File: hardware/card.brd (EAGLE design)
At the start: 160 x 100 mm, 56 parts, among them J1 UE27AC54100, J2 B2PS-VH(LF)(SN), J3 MINI-USB-UX60A-MB-5ST, J4 MICROSD, U1 ATSAMD21J_QFN, U3 TLV70233DBVR, U4 ATWINC1500_MR210PA, U5 NHD-C12832A1Z-FSW-FBW-3V3, U6 MIC2288YD5-TR, X3 32.768

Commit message: add framing for software components. Design review schematic tweaks
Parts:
- removed CN1: (no value), lib-card:JSTPH2
- removed T1: (no value), CardReader:SOT-23
- added C16, C23, C24: 10uF, rcl:C0603
- added C17, C18, C19, C20, C21: 0.1uF, rcl:C0603
- added C22, C25, C26, C27: 1uF, rcl:C0603
- added D7: RED, led:SMARTLED-TTW
- added F1: 2A, RoboJackets-Fuses:F0603
- added F2: 500mA, RoboJackets-Fuses:F0603
- added J5: JST_2PIN, CardReader:JSTPH2
- added R17: 2.2k, RoboJackets-Resistors:R0603W
- added R18: 100k, RoboJackets-Resistors:R0603W
- added R19: 10k, RoboJackets-Resistors:R0603W
- added U7: TS3USB221, CardReader:10-PIN-UQFN
- C14: value 4.7uF -> 10uF
- C15: value 22uF -> 10uF
- C9: value (none) -> 0.1uF
- J4: device lib-card:MICROSD -> CardReader:MICROSD
- R1, R2, R3: value 150 -> 330
- R16: value 10k -> 0; device rcl:R0603 -> RoboJackets-Resistors:R0603W
- R6, R8: value 100k 1% -> 10k 1%
- U1: device lib-card:TQFN48_7MM -> CardReader:TQFN48_7MM
- U2: value (none) -> MCP73833; device lib-card:MSOP10 -> CardReader:MSOP10
- U4: device lib-card:ATWINC1500_MR210PA -> CardReader:ATWINC1500_MR210PA
- moved R16 150.5 mm to (-61.5, -291.0)
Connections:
- removed net BOOST_ENABLE: R16.1, T1.1, U6.4
- new net 1D+: J3.3, U7.1
- new net 1D-: J3.2, U7.2
- new net 2D+: J1.3, U7.3
- new net 2D-: J1.2, U7.4
- new net BATT-PRE-FUSE: F1.2, J5.1
- new net N$11: C16.1, R16.1, U5.LED+
- new net N$13: R18.2, R19.2, U7.9
- new net PROG-LED: D7.A@1, R17.2
- new net PROG-LED-2: R17.1, U1.26
- net +3.3V: now also C21.1, C22.1, R16.2, U7.10; no longer U5.LED+
- net +5V: now also C26.1, C3.1, J3.1; no longer T1.3
- net BATT: now also C27.2, F1.1; no longer CN1.1
- net BTN-DOWN: now also C18.1
- net BTN-LEFT: now also C19.1
- net BTN-RIGHT: now also C20.1, U1.4; no longer U1.26
- net BTN-UP: now also C17.1
- net D+: now also U7.8; no longer J1.3, J3.3
- net D-: now also U7.7; no longer J1.2, J3.2
- net GND: now also C17.2, C18.2, C19.2, C20.2, C21.2, C22.2, C23.2, C24.2, C25.2, C26.2, C27.1, D7.C@1, J5.2, R18.1, U7.5, U7.6; no longer CN1.2, T1.2
- net N$27: now also U5.C1+
- net N$29: now also C15.1, C23.1, C24.1, D6.C, F2.1, R14.2; no longer C3.1, J3.1
- net USB-HOST-EN: now also R19.1
- net VBATT: now also C25.1, U6.4; no longer R16.2
- net VBUS: now also F2.2; no longer C15.1, D6.C, R14.2

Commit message: Schematic Finished
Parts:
- removed U5: NHD-C12832A1Z-FSW-FBW-3V3, CardReader:NHD-C12832A1Z-FSW-FBW-3V3
- added C28, C29, C30, C32: 0.1uF, rcl:C0603
- added C31: 1uF, rcl:C0603
- added J6: 0541323062, CardReader:0541323062
- added J7: JST_2PIN, card:JSTPH2
- added S6: KAE01SGGT, CardReader:KAE01SGGT
- C1, C10, C2, C8: value 0.1uF -> 1uF
- C11, C12, C13: value 2.2uF -> 0.1uF
- C16: value 10uF -> 1uF
- moved C1 315.6 mm to (-66.5, -386.0)
- moved C2 315.6 mm to (-66.5, -389.5)
- moved C8 315.6 mm to (-66.5, -393.0)
- moved C9 315.6 mm to (-66.5, -396.5)
- moved C11 312.1 mm to (-66.5, -400.0)
- moved C12 312.1 mm to (-66.5, -403.5)
- moved C13 312.1 mm to (-66.5, -407.0)
- moved C16 128.9 mm to (-76.5, -422.5)
- moved R16 128.9 mm to (-76.5, -419.0)
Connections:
- removed net N$11: C16.1, R16.1, U5.LED+
- removed net N$13: R18.2, R19.2, U7.9
- removed net N$19: C1.1, U5.V0
- removed net N$20: C8.1, U5.V2
- removed net N$21: C10.1, U5.V3
- removed net N$22: C2.1, U5.V1
- removed net N$23: C9.1, U5.V4
- removed net N$24: C11.1, U5.C2+
- removed net N$25: C11.2, U5.C2-
- removed net N$26: C13.1, U5.V_OUT
- removed net N$27: C12.1, U5.C1+
- removed net N$28: C12.2, U5.C1-
- removed net SCR-!CS: U1.25, U5.!CS1
- removed net SCR-!RST: U1.24, U5.!RST
- removed net SCR-REG: U1.16, U5.A0
- new net LCD-!CS: J6.1, U1.29
- new net LCD-!RES: J6.2, U1.31
- new net LCD-A0: J6.3, U1.48
- new net LCD-CA1+: C2.1, J6.18
- new net LCD-CA1-: C1.2, C2.2, J6.17
- new net LCD-CA2+: C8.1, J6.19
- new net LCD-CA2-: C8.2, J6.20
- new net LCD-CA3+: C1.1, J6.16
- new net LCD-K: J7.2, R16.1
- new net LCD-MOSI: J6.13, U1.37
- new net LCD-SCK: J6.12, U1.38
- new net LCD-V0: C28.1, J6.27
- new net LCD-V1: C13.1, J6.26
- new net LCD-V2: C12.1, J6.25
- new net LCD-V3: C11.1, J6.24
- new net LCD-V4: C9.1, J6.23
- new net LCD-VOUT: C10.1, J6.15
- new net USB-S: R18.2, R19.2, S6.1, U7.9
- net +3.3V: now also C16.1, C29.1, C30.1, C31.1, C32.1, J6.22, J6.4, J6.5, J7.1; no longer R16.2, U5.V_DD
- net BTN-LEFT: now also U1.25; no longer U1.29
- net BTN-RIGHT: now also U1.24; no longer U1.4
- net GND: now also C11.2, C12.2, C16.2, C28.2, C29.2, C30.2, C31.2, C32.2, J6.10, J6.11, J6.14, J6.21, J6.29, J6.30, J6.6, J6.7, J6.8, J6.9, R16.2, S6.2; no longer C1.2, C2.2, C8.2, U5.LED-, U5.V_SS
- net MOSI: no longer U5.SI
- net SCK: no longer U5.SCL

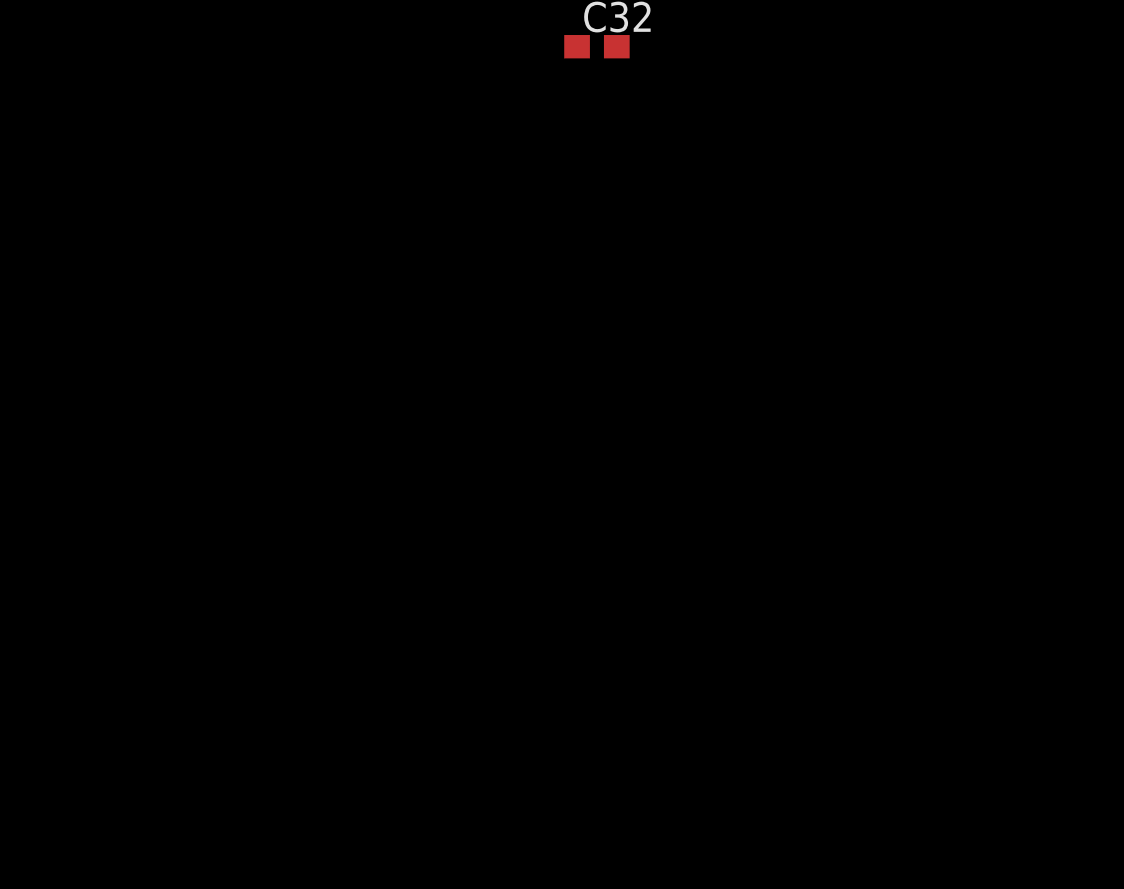
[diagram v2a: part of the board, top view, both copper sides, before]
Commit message: Added power test points and LEDs
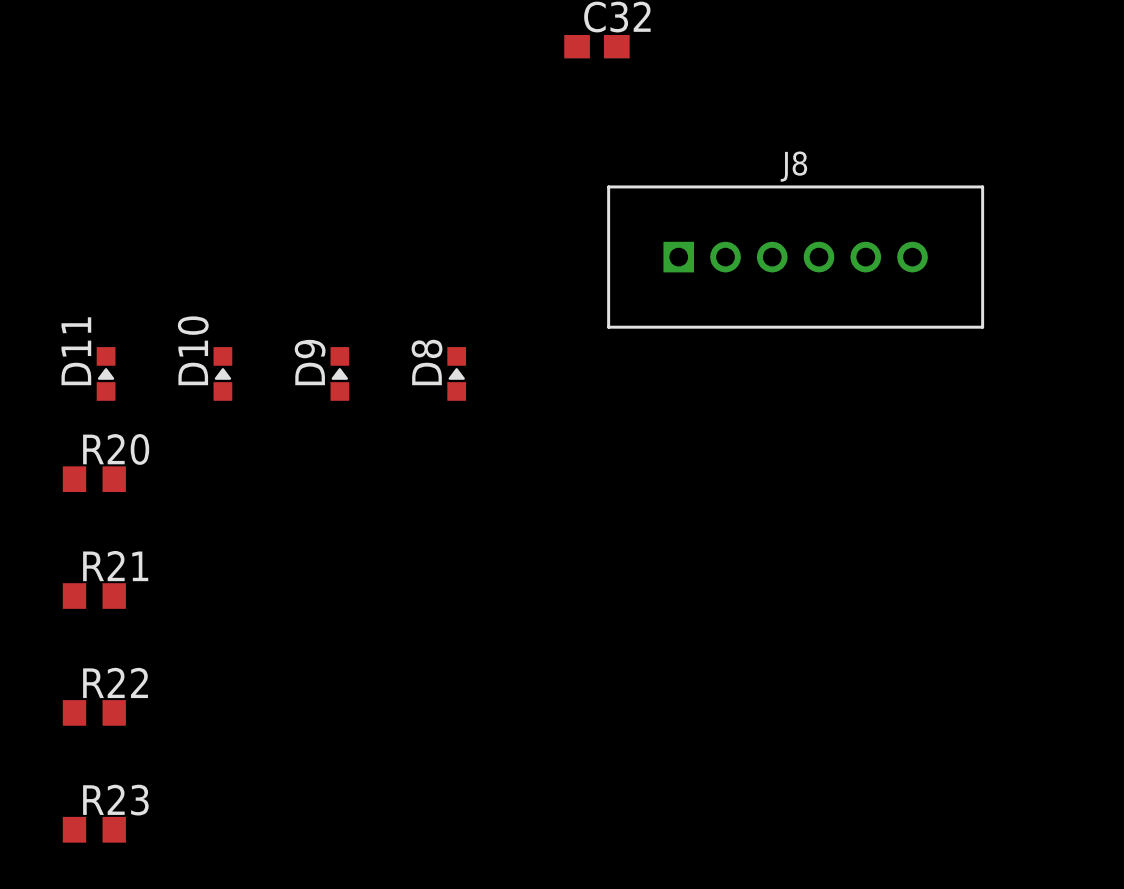
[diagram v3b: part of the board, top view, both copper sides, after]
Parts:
- added D10: YELLOW, lib-card:CHIP-LED0603
- added D11: RED, lib-card:CHIP-LED0603
- added D8, D9: GREEN, lib-card:CHIP-LED0603
- added J8: 6-PIN_2MM-V, RoboJackets-Connectors:2MM-6-V
- added R20, R21, R22, R23: 1k, rcl:R0603
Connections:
- net N$1 renamed LED-STAT2
- net N$14 renamed VDDCORE
- net N$15 renamed X3-1
- net N$16 renamed X3-2
- net N$17 renamed WIFI-LED-Y
- net N$18 renamed WIFI-LED-G
- net N$2 renamed LED-STAT1
- net N$29 renamed BOOST_OUTPUT
- net N$6 renamed LED-!PG
- new net LED-3V3: D9.A, R21.2
- new net LED-5V: D11.A, R23.2
- new net LED-VBATT: D10.A, R22.2
- new net LED-VBUS: D8.A, R20.2
- net +3.3V: now also J6.26, J6.27, J6.9, J8.3, R21.1; no longer J6.22, J6.4, J6.5
- net +5V: now also J8.6, R23.1
- net GND: now also D10.C, D11.C, D8.C, D9.C, J6.1, J6.17, J6.2, J6.20, J6.22, J6.23, J6.24, J6.25, J8.1; no longer J6.11, J6.14, J6.29, J6.30, J6.6, J6.7, J6.8, J6.9
- net LCD-!CS: now also J6.30; no longer J6.1
- net LCD-!RES: now also J6.29; no longer J6.2
- net LCD-A0: now also J6.28; no longer J6.3
- net LCD-CA1+: now also J6.13; no longer J6.18
- net LCD-CA1-: now also J6.14; no longer J6.17
- net LCD-CA2+: now also J6.12; no longer J6.19
- net LCD-CA2-: now also J6.11; no longer J6.20
- net LCD-CA3+: now also J6.15; no longer J6.16
- net LCD-MOSI: now also J6.18; no longer J6.13
- net LCD-SCK: now also J6.19; no longer J6.12
- net LCD-V0: now also J6.4; no longer J6.27
- net LCD-V1: now also J6.5; no longer J6.26
- net LCD-V2: now also J6.6; no longer J6.25
- net LCD-V3: now also J6.7; no longer J6.24
- net LCD-V4: now also J6.8; no longer J6.23
- net LCD-VOUT: now also J6.16; no longer J6.15
- net VBATT: now also J8.4, R22.1
- net VBUS: now also J8.5, R20.1

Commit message: halfway through routing
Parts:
- D11: value RED -> GREEN
- D8: value GREEN -> RED
- moved R23 532.3 mm to (27.5, 39.5), flipped to the bottom, turned to 270 degrees
- moved R22 526.4 mm to (23.5, 39.5), flipped to the bottom, turned to 270 degrees
- moved R21 521.1 mm to (21.5, 39.5), flipped to the bottom, turned to 270 degrees
- moved C31 518.9 mm to (45.0, 67.0), flipped to the bottom, turned to 270 degrees
- moved R20 517.2 mm to (25.5, 39.5), flipped to the bottom, turned to 270 degrees
- moved C30 514.4 mm to (46.5, 67.0), flipped to the bottom, turned to 270 degrees
- moved C29 512.7 mm to (55.0, 68.0), flipped to the bottom, turned to 180 degrees
- moved C16 509.3 mm to (55.0, 69.5), flipped to the bottom, turned to 180 degrees
- moved D11 508.0 mm to (27.5, 34.0), flipped to the bottom, turned to 180 degrees
- moved S6 505.7 mm to (56.0, 54.0), flipped to the bottom
- moved D10 505.7 mm to (23.5, 34.0), flipped to the bottom, turned to 180 degrees
- moved J8 504.5 mm to (21.5, 43.5)
- moved D9 504.0 mm to (21.5, 34.0), flipped to the bottom, turned to 180 degrees
- moved D8 503.8 mm to (25.5, 34.0), flipped to the bottom, turned to 180 degrees
- moved C32 472.1 mm to (37.0, 14.0), turned to 90 degrees
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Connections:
- net N$10 renamed WIFI-GPIO15
- net N$3 renamed CHRG-STAT1
- net N$4 renamed CHRG-STAT2
- net N$5 renamed CHRG-!PG
- net N$7 renamed CHRG-PROG
- net N$8 renamed CHRG-THERM
- removed net N$9: R11.2, U4.J27
- new net WIFI-GPIO16: R11.1, U4.J27
- net +5V: now also J8.5, R20.1; no longer J8.6, R23.1
- net VBUS: now also J8.6, R23.1; no longer J8.5, R20.1
- net WIFI-LED-Y: now also R11.2; no longer R11.1
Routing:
- net +3.3V: track 0.00 -> 82.3 mm, vias 0 -> 5
- net WIFI-!IRQ: track 0.00 -> 77.6 mm, vias 0 -> 3
- net GND: track 0.00 -> 75.2 mm, vias 0 -> 22
- net WIFI-CHIP-EN: track 0.00 -> 73.9 mm, vias 0 -> 1
- net VBATT: track 0.00 -> 70.0 mm, vias 0 -> 2
- net +5V: track 0.00 -> 67.9 mm, vias 0 -> 3
- net 1D+: track 0.00 -> 47.6 mm, vias 0 -> 1
- net 1D-: track 0.00 -> 46.2 mm, vias 0 -> 1
- net BATT: track 0.00 -> 40.5 mm, vias 0 -> 1
- net LCD-!RES: track 0.00 -> 33.5 mm
- net LCD-!CS: track 0.00 -> 30.7 mm
- net 2D-: track 0.00 -> 29.9 mm
- net 2D+: track 0.00 -> 27.6 mm
- net USB-HOST-EN: track 0.00 -> 16.3 mm, vias 0 -> 1
- net BOOST_OUTPUT: track 0.00 -> 14.6 mm
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- added copper zone on layer 16, net GND
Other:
- board size 160 x 100 mm -> 100 x 100 mm

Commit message: basically done routing attempt 1
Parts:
- moved J4 7.00 mm to (33.1, 80.9)
- moved C21 7.00 mm to (26.5, 87.0)
- moved C22 7.00 mm to (26.5, 85.0)
- moved C19 5.15 mm to (77.0, 66.5)
- moved C20 4.27 mm to (92.0, 66.5), turned to 180 degrees
- moved R16 3.64 mm to (59.5, 16.5), turned to 90 degrees
- moved C18 2.69 mm to (83.5, 57.5), turned to 270 degrees
- moved C17 1.12 mm to (84.0, 82.5), turned to 90 degrees
- moved R9 1.12 mm to (12.7, 2.92)
- moved C32 0.56 mm to (36.8, 13.5)
- moved U4 0.14 mm to (8.25, 13.5)
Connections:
- net BTN-LEFT: now also U1.27; no longer U1.25
- net BTN-RIGHT: now also U1.25; no longer U1.24
- net BTN-UP: now also U1.24; no longer U1.27
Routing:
- net +3.3V: track 82.3 -> 252.1 mm, vias 5 -> 16
- net MOSI: track 6.57 -> 107.5 mm, vias 1 -> 6
- net VBUS: track 3.15 -> 101.4 mm, vias 0 -> 6
- net MISO: track 6.57 -> 102.7 mm, vias 1 -> 6
- net SCK: track 6.98 -> 101.2 mm, vias 1 -> 6
- net WIFI-!CS: track 0.00 -> 79.3 mm, vias 0 -> 5
- net LCD-A0: track 6.22 -> 72.0 mm, vias 0 -> 2
- net BTN-DOWN: track 3.02 -> 64.2 mm, vias 1 -> 3
- net BTN-UP: track 3.98 -> 64.7 mm, vias 1 -> 3
- net BTN-RIGHT: track 2.19 -> 60.9 mm, vias 1 -> 3
- net LCD-SCK: track 9.41 -> 62.6 mm
- net LCD-MOSI: track 8.41 -> 61.6 mm
- net BTN-LEFT: track 1.48 -> 49.3 mm, vias 1 -> 3
- net SD-!CS: track 0.00 -> 31.7 mm, vias 0 -> 1
- net LCD-!CS: track 30.7 -> 59.4 mm, vias 0 -> 2
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
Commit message: board routing attempt 2
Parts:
- removed U6: MIC2288YD5-TR, CardReader:TSOT-23-5
- removed U7: TS3USB221, CardReader:10-PIN-UQFN
- added C33: 1uF, rcl:C0603
- added U5: TLV70233DBVR, lib-card:SOT-23-5
- added X2: 32.768, lib-card:XTAL3215
- C1, C16, C2, C25: value 1uF -> 0.1uF
- C10, C8: value 1uF -> 22pF
- C14, C15: value 10uF -> 0.1uF
- C19, C30, C32, C9: value 0.1uF -> 1uF
- C23, C24: value 10uF -> 1uF
- C26, C27: value 1uF -> 10uF
- C28, C29: value 0.1uF -> 10uF
- C3: value 10uF -> 1uF; device rcl:C0805 -> rcl:C0603
- C6: value 22pF -> 0.1uF
- C7: value 22pF -> 10uF; device rcl:C0603 -> rcl:C0805
- D1, D11: value GREEN -> RED; device lib-card:CHIP-LED0603 -> RoboJackets-LEDs:CHIP-LED0603
- D10, D2, D9: device lib-card:CHIP-LED0603 -> RoboJackets-LEDs:CHIP-LED0603
- D3, D8: value RED -> GREEN; device lib-card:CHIP-LED0603 -> RoboJackets-LEDs:CHIP-LED0603
- D4: value YELLOW -> PMEG4010EGWX; device led:SMARTLED-TTW -> CardReader:SOD123
- D5: device led:SMARTLED-TTW -> RoboJackets-LEDs:CHIP-LED0603
- D6: value PMEG4010EGWX -> GREEN; device CardReader:SOD123 -> RoboJackets-LEDs:CHIP-LED0603
- D7: value RED -> GREEN; device led:SMARTLED-TTW -> RoboJackets-LEDs:CHIP-LED0603
- F1: value 2A -> 500mA
- F2: value 500mA -> 2A
- J2: value B2PS-VH(LF)(SN) -> MICROSD; device RoboJackets-Connectors:B2PS-CENTERED -> CardReader:MICROSD
- J3: value MINI-USB-UX60A-MB-5ST -> 0541323062; device lib-card:UX60A-MB-5ST -> CardReader:0541323062
- J4: value MICROSD -> 6-PIN_2MM-V; device CardReader:MICROSD -> RoboJackets-Connectors:2MM-6-V
- J6: value 0541323062 -> B2PS-VH(LF)(SN); device CardReader:0541323062 -> RoboJackets-Connectors:B2PS-CENTERED
- J7: value JST_2PIN -> MINI-USB-UX60A-MB-5ST; device card:JSTPH2 -> lib-card:UX60A-MB-5ST
- J8: value 6-PIN_2MM-V -> JST_2PIN; device RoboJackets-Connectors:2MM-6-V -> card:JSTPH2
- R1: value 330 -> 10k
- R10, R9: value 100k -> 1k; device RoboJackets-Resistors:R0603W -> rcl:R0603
- R11, R12, R19: device RoboJackets-Resistors:R0603W -> rcl:R0603
- R13: value 0 -> 5.62k 1%
- R14: value 5.62k 1% -> 1.87k 1%
- R15: value 1.87k 1% -> 10k 1%
- R16: value 0 -> 10k 1%; device RoboJackets-Resistors:R0603W -> rcl:R0603
- R17: value 2.2k -> 330; device RoboJackets-Resistors:R0603W -> rcl:R0603
- R18: value 100k -> 330; device RoboJackets-Resistors:R0603W -> rcl:R0603
- R2: value 330 -> 100k
- R21, R4: value 1k -> 0
- R22: value 1k -> 10k
- R23: value 1k -> 330
- R3: value 330 -> 2.2k
- R5: value 10k -> 100k
- R6: value 10k 1% -> 1k
- R7: value 10k -> 1k
- R8: value 10k 1% -> 100k
- S2: value TL1000F160Q -> KAE01SGGT; device CardReader:TL1100 -> CardReader:KAE01SGGT
- S6: value KAE01SGGT -> TL1000F160Q; device CardReader:KAE01SGGT -> CardReader:TL1100
- U2: value MCP73833 -> TS3USB221; device CardReader:MSOP10 -> CardReader:10-PIN-UQFN
- U3: value TLV70233DBVR -> MIC2288YD5-TR; device lib-card:SOT-23-5 -> CardReader:TSOT-23-5
- U4: value ATWINC1500_MR210PA -> MCP73833; device CardReader:ATWINC1500_MR210PA -> CardReader:MSOP10
- X3: value 32.768 -> ATWINC1500_MR210PA; device lib-card:XTAL3215 -> CardReader:ATWINC1500_MR210PA
- moved S2 98.6 mm to (27.5, 5.00), turned to 90 degrees
- moved C22 89.3 mm to (74.2, 9.50)
- moved S5 89.2 mm to (13.0, 31.5), flipped to the bottom
- moved C21 89.2 mm to (80.5, 16.0), turned to 90 degrees
- moved J2 87.9 mm to (82.2, 21.8), flipped to the top, turned to 0 degrees
- moved R4 79.8 mm to (92.0, 18.0), turned to 90 degrees
- moved R9 79.2 mm to (86.2, 32.5), turned to 90 degrees
- moved D6 79.1 mm to (92.8, 33.8)
- moved J8 77.6 mm to (91.0, 9.00), flipped to the bottom, turned to 180 degrees
- moved J4 76.5 mm to (89.2, 29.0), flipped to the top, turned to 180 degrees
- moved C23 76.3 mm to (75.8, 13.0)
- moved C25 72.7 mm to (70.8, 16.0)
- moved R11 72.4 mm to (89.5, 32.5), turned to 90 degrees
- moved J3 71.9 mm to (75.0, 11.0), flipped to the bottom
- moved C24 71.3 mm to (74.2, 16.0), flipped to the bottom, turned to 90 degrees
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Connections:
- net !RESET: now also C6.1
- net +3.3V: now also C1.1, C11.1, C2.1, C25.1, C3.1, C33.1, C9.1, D2.A, D3.A, J2.4, J3.22, J3.4, J3.5, J4.3, J8.1, R10.1, U2.10, U5.5, X3.J10, X3.J20, X3.J23; no longer C16.1, C21.1, C22.1, C29.1, C30.1, C31.1, C32.1, D4.A@1, D5.A@1, J4.4, J6.26, J6.27, J6.9, J7.1, J8.3, R21.1, U3.5, U4.J10, U4.J20, U4.J23, U7.10
- net +5V: now also C31.1, C7.1, D10.A, D11.A, D9.A, J4.5, J7.1, R9.1, U4.1, U4.2; no longer C26.1, C3.1, D1.A, D2.A, D3.A, J3.1, J8.5, R20.1, U2.1, U2.2
- net 1D+: now also J7.3, U2.1; no longer J3.3, U7.1
- net 1D-: now also J7.2, U2.2; no longer J3.2, U7.2
- net 2D+: now also U2.3; no longer U7.3
- net 2D-: now also U2.4; no longer U7.4
- net 3V3_EN: now also R19.1, U5.3; no longer R7.1, U3.3
- net BATT: now also C32.2, F2.1, J6.2, R21.1, U4.10, U4.9; no longer C27.2, F1.1, J2.2, R13.1, U2.10, U2.9
- net BATT-MONITOR: now also R15.2, R16.1; no longer R6.2, R8.1
- net BATT-PRE-FUSE: now also F2.2; no longer F1.2
- net BOOST_FB: now also R13.1, R14.2, U3.3; no longer R14.1, R15.2, U6.3
- net BOOST_OUTPUT: now also C27.1, C28.1, C29.1, D4.C, F1.1, R13.2; no longer C15.1, C23.1, C24.1, D6.C, F2.1, R14.2
- net BOOST_SW: now also D4.A, U3.1; no longer D6.A, U6.1
- net BTN-DOWN: now also C13.1, S4.1, U1.3; no longer C18.1, S3.1, S3.2, U1.28
- net BTN-LEFT: now also C14.1, S5.1, U1.7; no longer C19.1, S4.1, S4.2, U1.27
- net BTN-RIGHT: now also C15.1, S6.2, U1.8; no longer C20.1, S5.1, S5.2, U1.25
- net BTN-UP: now also C12.1, S3.1, U1.10; no longer C17.1, S2.1, S2.2, U1.24
- net CHRG-!PG: now also R23.1, U4.7; no longer R3.1, U2.7
- net CHRG-PROG: now also R20.2, U4.6; no longer R4.2, U2.6
- net CHRG-STAT1: now also R18.1, U4.3; no longer R2.1, U2.3
- net CHRG-STAT2: now also R17.1, U4.4; no longer R1.1, U2.4
- net CHRG-THERM: now also R22.2, U4.8; no longer R5.2, U2.8
- net D+: now also U2.8; no longer U7.8
- net D-: now also U2.7; no longer U7.7
- net GND: now also C1.2, C2.2, C27.2, C32.1, C33.2, C8.2, D1.C, D5.C, D6.C, D7.C, J2.6, J2.MT1, J2.MT2, J3.10, J3.11, J3.14, J3.21, J3.29, J3.30, J3.6, J3.7, J3.8, J3.9, J4.1, J7.5, R14.1, R2.1, R20.1, R22.1, R4.2, R5.2, R8.1, S2.2, S6.3, S6.4, U2.6, U4.5, U5.2, X3.J12, X3.J28, X3.J9; no longer C19.2, C22.2, C23.2, C27.1, C32.2, D10.C, D11.C, D7.C@1, D9.C, J3.5, J4.6, J4.MT1, J4.MT2, J6.1, J6.10, J6.17, J6.2, J6.20, J6.21, J6.22, J6.23, J6.24, J6.25, J8.1, R10.2, R15.1, R18.1, R4.1, R5.1, R8.2, R9.1, S2.3, S2.4, S6.2, U4.J12, U4.J28, U4.J9, U6.2, U7.5, U7.6
- net LCD-!CS: now also J3.1, U1.23; no longer J6.30, U1.29
- net LCD-!RES: now also J3.2, U1.24; no longer J6.29, U1.31
- net LCD-A0: now also J3.3, U1.25; no longer J6.28, U1.48
- net LCD-CA1+: now also C22.1, J3.18; no longer C2.1, J6.13
- net LCD-CA1-: now also C22.2, C23.2, J3.17; no longer C1.2, C2.2, J6.14
- net LCD-CA2+: now also C19.1, J3.19; no longer C8.1, J6.12
- net LCD-CA2-: now also C19.2, J3.20; no longer C8.2, J6.11
- net LCD-CA3+: now also C23.1, J3.16; no longer C1.1, J6.15
- net LCD-K: now also J8.2, R4.1; no longer J7.2, R16.1
- net LCD-MOSI: now also J3.13; no longer J6.18
- net LCD-SCK: now also J3.12; no longer J6.19
- net LCD-V0: now also C18.1, J3.27; no longer C28.1, J6.4
- net LCD-V1: now also C21.1, J3.26; no longer C13.1, J6.5
- net LCD-V2: now also C17.1, J3.25; no longer C12.1, J6.6
- net LCD-V3: now also C20.1, J3.24; no longer C11.1, J6.7
- net LCD-V4: now also C16.1, J3.23; no longer C9.1, J6.8
- net LCD-VOUT: now also C24.1, J3.15; no longer C10.1, J6.16
- net LED-!PG: now also D11.C, R23.2; no longer D3.C, R3.2
- net LED-3V3: now also D6.A, R10.2; no longer D9.A, R21.2
- net LED-5V: now also D8.A, R12.2; no longer D11.A, R23.2
- net LED-STAT1: now also D10.C, R18.2; no longer D2.C, R2.2
- net LED-STAT2: now also D9.C, R17.2; no longer D1.C, R1.2
- net LED-VBATT: now also D7.A, R11.2; no longer D10.A, R22.2
- net LED-VBUS: now also D5.A, R9.2; no longer D8.A, R20.2
- net MISO: now also J2.7, X3.J17; no longer J4.7, U4.J17
- net MOSI: now also J2.3, X3.J15; no longer J4.3, U4.J15
- net PROG-LED: now also D1.A, R3.2; no longer D7.A@1, R17.2
- net PROG-LED-2: now also R3.1; no longer R17.1
- net SCK: now also J2.5, X3.J18; no longer J4.5, U4.J18
- net SD-!CD: now also J2.CD1, U1.16; no longer J4.CD1, U1.14
- net SD-!CS: now also J2.2, U1.27; no longer J4.2, U1.12
- net USB-HOST-EN: now also R1.1; no longer R19.1
- net USB-S: now also R1.2, R2.2, S2.1, U2.9; no longer R18.2, R19.2, S6.1, U7.9
- net VBATT: now also C26.1, C30.1, J4.4, J6.1, R11.1, R15.1, R19.2, R21.2, U3.4, U3.5, U5.1; no longer C14.1, C25.1, J2.1, J8.4, R13.2, R22.1, R6.1, R7.2, U3.1, U6.4, U6.5
- net VBUS: now also F1.2, J4.6, R12.1; no longer F2.2, J8.6, R23.1
- net WIFI-!CS: now also X3.J16; no longer U4.J16
- net WIFI-!IRQ: now also U1.14, X3.J13; no longer U1.30, U4.J13
- net WIFI-!RESET: now also R8.2, X3.J4; no longer R9.2, U4.J4
- net WIFI-CHIP-EN: now also R5.1, U1.12, X3.J22; no longer R10.1, U1.23, U4.J22
- net WIFI-GPIO15: now also R7.2, X3.J26; no longer R12.2, U4.J26
- net WIFI-GPIO16: now also R6.1, X3.J27; no longer R11.1, U4.J27
- net WIFI-LED-G: now also D3.C, R7.1; no longer D5.C@1, R12.1
- net WIFI-LED-Y: now also D2.C, R6.2; no longer D4.C@1, R11.2
- net WIFI-WAKE: now also X3.J11; no longer U4.J11
- net X3-1: now also C8.1, X2.P$1; no longer C6.1, X3.P$1
- net X3-2: now also C10.1, X2.P$2; no longer C7.1, X3.P$2
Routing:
- net +3.3V: track 252.1 -> 151.5 mm, vias 16 -> 14
- net MISO: track 102.7 -> 37.1 mm, vias 6 -> 2
- net MOSI: track 107.5 -> 42.8 mm, vias 6 -> 4
- net +5V: track 67.9 -> 131.4 mm
- net SCK: track 101.2 -> 38.1 mm, vias 6 -> 2
- net WIFI-!CS: track 79.3 -> 16.9 mm, vias 5 -> 2
- net VBUS: track 101.4 -> 40.2 mm, vias 6 -> 0
- net USB-S: track 8.69 -> 68.5 mm, vias 0 -> 4
- net WIFI-!IRQ: track 77.6 -> 17.9 mm, vias 3 -> 2
- net !RESET: track 14.3 -> 70.5 mm, vias 1 -> 4
- net WIFI-CHIP-EN: track 73.7 -> 19.4 mm, vias 1 -> 2
- net LCD-A0: track 72.0 -> 17.8 mm, vias 2 -> 1
- net GND: track 64.6 -> 16.9 mm, vias 28 -> 11
- net LCD-!RES: track 60.9 -> 16.0 mm, vias 2 -> 1
- net LCD-!CS: track 59.4 -> 16.2 mm, vias 2 -> 1
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- added copper zone on layer 1, net GND
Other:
- board size 100 x 100 mm -> 97 x 56 mm
- board text added: "+3.3V"
- board text added: "+5V"
- board text added: "VBAT"
- board text added: "VBUS"
